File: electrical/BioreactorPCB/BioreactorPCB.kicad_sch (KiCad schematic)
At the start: 28 parts, among them IC1 AL5809-20P1-7, J1 61300311121, J12 Conn_02x03_Odd_Even, J2 61300311121, J3 Conn_01x05_Male, J4 Conn_01x06_Male, J6 OSTTC022162, J8 OSTTC042162, Q1 2N3905, Q2 IRF4905, U3 ATMEGA328P-AUR, U5 ATmega328PB-M, Y1 16 mHz

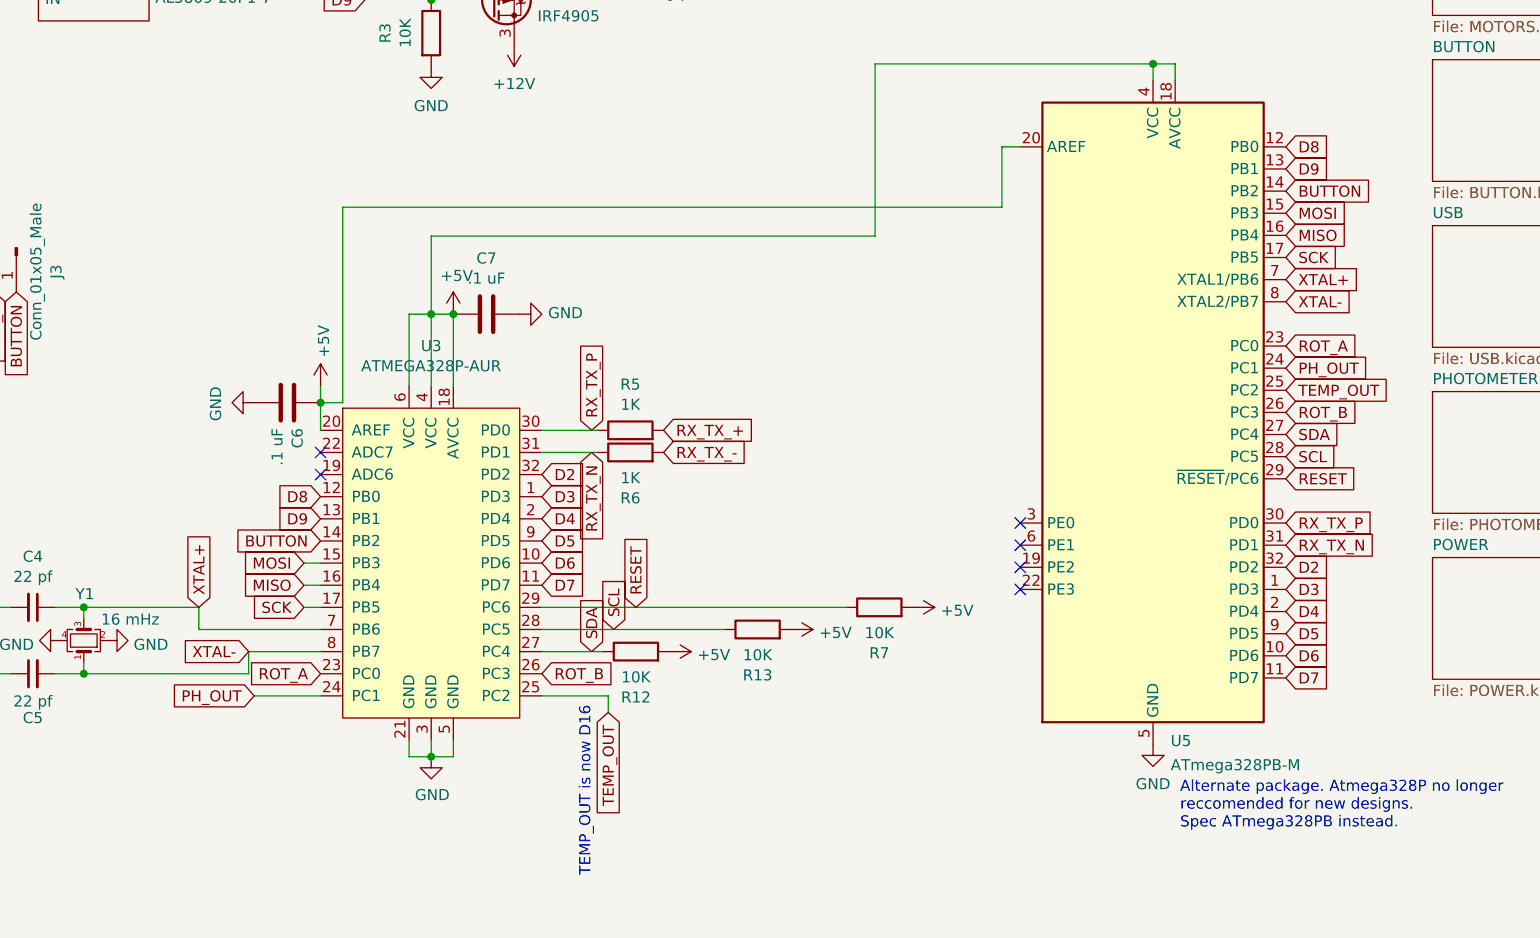
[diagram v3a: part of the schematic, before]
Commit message: NOW a 4-layer pCB with drastically improved routing
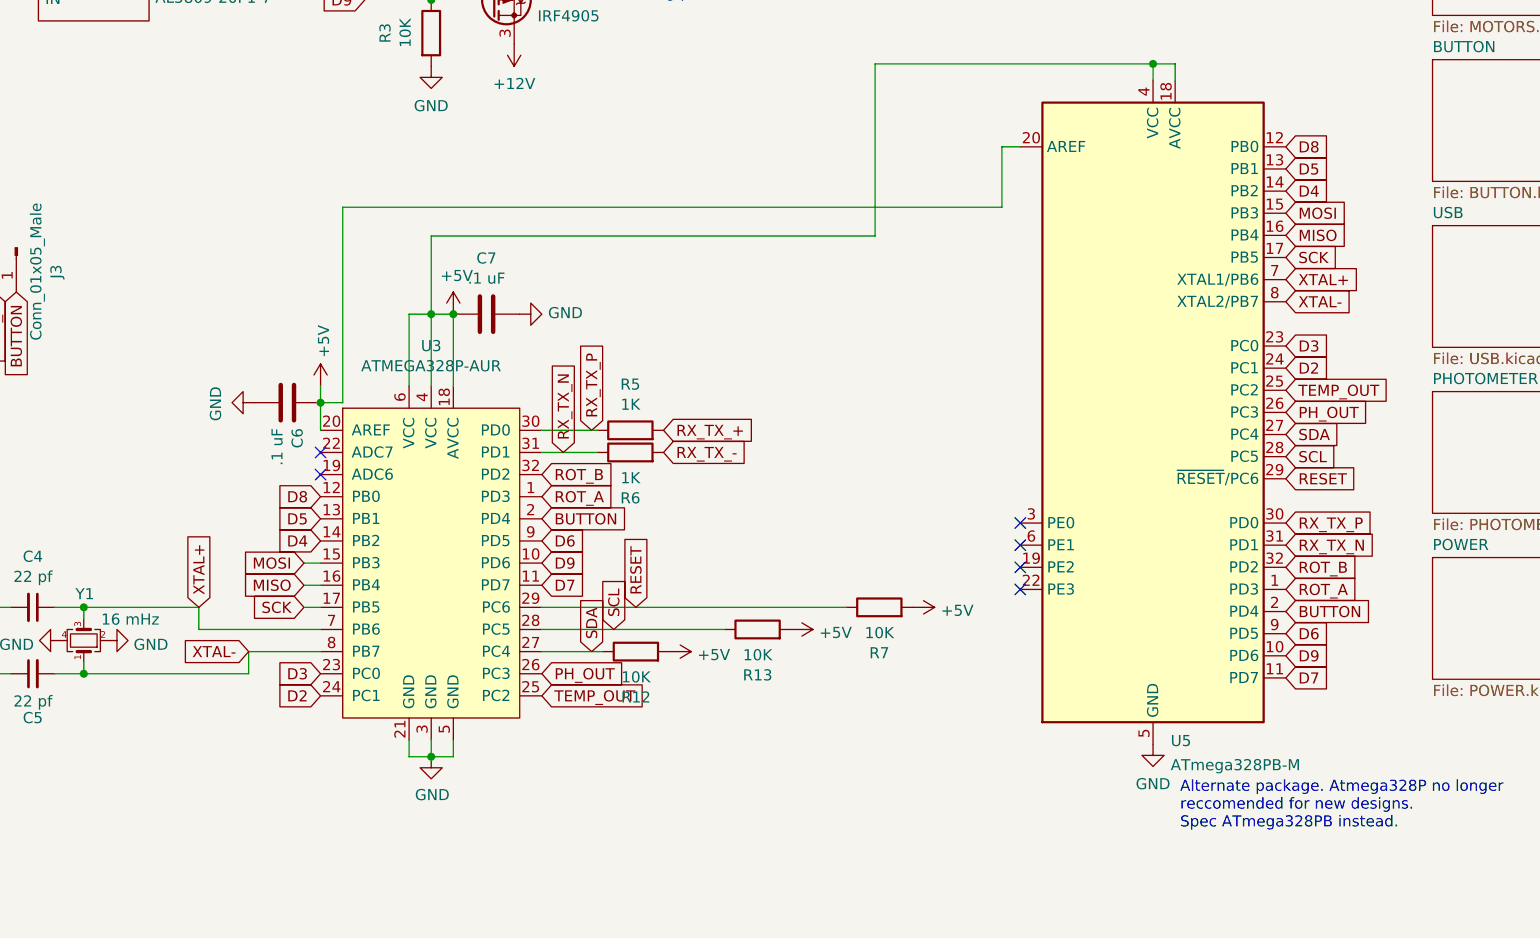
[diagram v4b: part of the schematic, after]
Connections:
- net BUTTON: now also U3.2 (PD4), U5.2 (PD4); no longer U3.14 (PB2), U5.14 (PB2)
- net D2: now also U3.24 (PC1), U5.24 (PC1); no longer U3.32 (PD2), U5.32 (PD2)
- net D3: now also U3.23 (PC0), U5.23 (PC0); no longer U3.1 (PD3), U5.1 (PD3)
- net D4: now also U3.14 (PB2), U5.14 (PB2); no longer U3.2 (PD4), U5.2 (PD4)
- net D5: now also U3.13 (PB1), U5.13 (PB1); no longer U3.9 (PD5), U5.9 (PD5)
- net D6: now also U3.9 (PD5), U5.9 (PD5); no longer U3.10 (PD6), U5.10 (PD6)
- net D9: now also U3.10 (PD6), U5.10 (PD6); no longer U3.13 (PB1), U5.13 (PB1)
- net PH_OUT: now also U3.26 (PC3), U5.26 (PC3); no longer U3.24 (PC1), U5.24 (PC1)
- net ROT_A: now also U3.1 (PD3), U5.1 (PD3); no longer U3.23 (PC0), U5.23 (PC0)
- net ROT_B: now also U3.32 (PD2), U5.32 (PD2); no longer U3.26 (PC3), U5.26 (PC3)
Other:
- note removed: "TEMP_OUT is now D16"
